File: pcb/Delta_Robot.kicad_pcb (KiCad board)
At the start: 2 copper layers, 151 parts, among them J1 Conn_01x04, J2 USB_A, J3 USB_A, J4 Conn_01x02, J5 Conn_01x02, J6 MP3V5050VC6U, Q1 IRF9540STRLPBF, Q2 IRF9540STRLPBF, SW1 TL3305A, SW2 TL3305A, SW3 TL3305A, SW4 TL3305A, U1 LDL1117S33R, U2 LDL1117S33R, U3 ZLDO1117G12TA, U4 ICE40UP5K-SG48I, U5 W25Q16JVSSIQ TR, U5 W25Q64JVSSIQ, U6 STM32F412RGT6, U7 Omega2+, U8 4N25-X007T, U9 4N25-X007T, Y1 Crystal

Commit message: Organizacion basica PCB
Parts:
- removed the C16 at (174.4, 124.6)
- removed the C16 at (136.3, 168.8)
- removed the C17 at (170.0, 127.1)
- removed the C17 at (145.6, 157.0)
- removed the C18 at (165.7, 127.1)
- removed the C18 at (141.2, 159.5)
- removed the C19 at (177.0, 117.8)
- removed the C19 at (136.3, 166.3)
- removed the C20 at (178.8, 122.8)
- removed the C20 at (136.9, 162.0)
- removed the C21 at (174.4, 127.1)
- removed the C21 at (131.9, 168.8)
- removed the C22 at (177.0, 120.3)
- removed the C22 at (136.9, 159.5)
- removed the C23 at (170.1, 124.6)
- removed the C23 at (131.9, 166.3)
- removed the D3 at (157.0, 123.1)
- removed the D3 at (129.5, 152.4)
- removed the D5 at (76.1, 135.8)
- removed the D7 at (116.4, 54.8)
- removed the D7 at (164.3, 158.0)
- removed L11: 742792651, Inductor_SMD:L_0603_1608Metric_Pad1.05x0.95mm_HandSolder
- removed the R3 at (161.4, 124.6)
- removed the R4 at (157.0, 125.6)
- removed the R5 at (177.0, 115.3)
- removed the R6 at (165.7, 124.6)
- removed the R7 at (161.3, 127.1)
- removed the R7 at (145.6, 162.0)
- removed the SW1 at (91.4, 131.5)
- removed the SW2 at (129.7, 49.5)
- removed the SW2 at (156.9, 158.7)
- removed the SW3 at (119.4, 49.5)
- removed the U4 at (170.2, 118.7)
- removed the U5 at (160.2, 117.9)
- added C16: 0.1uF, Capacitor_SMD:C_0603_1608Metric, F.Cu at (87.7, 93.2)
- added C17: 1uF, Capacitor_SMD:C_0603_1608Metric, F.Cu at (102.9, 69.8)
- added C18: 1uF, Capacitor_SMD:C_0603_1608Metric, F.Cu at (106.9, 81.4)
- added C19: 1uF, Capacitor_SMD:C_0603_1608Metric, F.Cu at (100.5, 85.7)
- added C20: 1uF, Capacitor_SMD:C_0603_1608Metric, F.Cu at (87.6, 73.0)
- added C21: 0.1uF, Capacitor_SMD:C_0603_1608Metric, F.Cu at (99.9, 69.8)
- added C22: 0.1uF, Capacitor_SMD:C_0603_1608Metric, F.Cu at (106.9, 78.5)
- added C23: 10uF, Capacitor_SMD:C_0603_1608Metric, F.Cu at (106.9, 87.4)
- added C51: 100nF, Capacitor_SMD:C_0603_1608Metric, F.Cu at (53.0, 44.2)
- added C52: 100nF, Capacitor_SMD:C_0603_1608Metric, F.Cu at (48.5, 44.2)
- added C53: 1uF, Capacitor_SMD:C_0603_1608Metric, F.Cu at (57.4, 44.2)
- added D3: CDBU0520, Diode_SMD:D_0603_1608Metric, F.Cu at (103.0, 85.7)
- added D7: NUP2105L, Package_TO_SOT_SMD:SOT-23, F.Cu at (113.3, 43.2)
- added J7: RJ45, Connector_RJ:RJ45_Amphenol_RJHSE5380, F.Cu at (56.8, 30.5)
- added R32: 50, Resistor_SMD:R_0603_1608Metric, F.Cu at (54.5, 40.9)
- added R33: 50, Resistor_SMD:R_0603_1608Metric, F.Cu at (48.5, 40.9)
- added R34: 50, Resistor_SMD:R_0603_1608Metric, F.Cu at (51.6, 40.9)
- added R35: 50, Resistor_SMD:R_0603_1608Metric, F.Cu at (57.4, 40.9)
- added R7: 100, Resistor_SMD:R_0603_1608Metric, F.Cu at (106.9, 84.3)
- added SW2: TL3305A, Button_Switch_SMD:SW_SPST_TL3305A, F.Cu at (120.9, 65.4)
- C1, C2, C24, C25, C26, C27, C28, C29, C30, C31, C34, C35, C38, C39, C40, C42, C43, C44, C45, C46, C47, C48, C49, C50, C7, C8: footprint Capacitor_SMD:C_0603_1608Metric_Pad1.05x0.95mm_HandSolder -> Capacitor_SMD:C_0603_1608Metric
- C10, C11: value 220u -> 220uF; footprint Capacitor_SMD:C_0603_1608Metric_Pad1.05x0.95mm_HandSolder -> Capacitor_SMD:C_0603_1608Metric
- C12, C13, C33, C36, C37, C4, C5, C6: value 0.1u -> 0.1uF; footprint Capacitor_SMD:C_0603_1608Metric_Pad1.05x0.95mm_HandSolder -> Capacitor_SMD:C_0603_1608Metric
- C14, C15: value 1n -> 1nF; footprint Capacitor_SMD:C_0603_1608Metric_Pad1.05x0.95mm_HandSolder -> Capacitor_SMD:C_0603_1608Metric
- C3, C9: value 33u -> 33uF; footprint Capacitor_SMD:C_0603_1608Metric_Pad1.05x0.95mm_HandSolder -> Capacitor_SMD:C_0603_1608Metric
- C32: value 22u -> 22uF; footprint Capacitor_SMD:C_0603_1608Metric_Pad1.05x0.95mm_HandSolder -> Capacitor_SMD:C_0603_1608Metric
- C41: value 0.01uF -> 10nF; footprint Capacitor_SMD:C_0603_1608Metric_Pad1.05x0.95mm_HandSolder -> Capacitor_SMD:C_0603_1608Metric
- D1, D10, D2, D8: footprint LED_SMD:LED_0603_1608Metric_Pad1.05x0.95mm_HandSolder -> LED_SMD:LED_0603_1608Metric
- D11, D9: footprint Diode_SMD:D_0603_1608Metric_Pad1.05x0.95mm_HandSolder -> Diode_SMD:D_0603_1608Metric
- L1, L10, L2, L3, L4, L5, L6: footprint Inductor_SMD:L_0603_1608Metric_Pad1.05x0.95mm_HandSolder -> Inductor_SMD:L_0603_1608Metric
- R1, R10, R11, R12, R13, R14, R15, R16, R17, R18, R19, R2, R20, R21, R22, R23, R24, R25, R26, R27, R29, R30, R31, R8, R9: footprint Resistor_SMD:R_0603_1608Metric_Pad1.05x0.95mm_HandSolder -> Resistor_SMD:R_0603_1608Metric
- U7: footprint Module:Onion_Omega2+ -> TH:ONION_OMEGA2
- moved H2 211.6 mm to (17.8, 25.4), turned to 180 degrees
- moved H4 202.7 mm to (17.4, 92.8)
- moved R25 201.1 mm to (25.4, 81.7)
- moved L10 196.8 mm to (18.0, 84.8), turned to 180 degrees
- moved R22 195.3 mm to (37.0, 81.7)
- moved R21 195.2 mm to (35.4, 62.6)
- moved R24 194.7 mm to (35.4, 59.6), turned to 180 degrees
- moved R23 194.6 mm to (35.5, 53.2)
- moved J4 184.4 mm to (38.6, 90.3)
- moved J5 183.7 mm to (27.1, 90.3)
- moved R20 181.2 mm to (48.9, 53.2)
- moved U9 180.2 mm to (28.4, 57.9), turned to 180 degrees
- moved U8 176.1 mm to (42.4, 57.9), turned to 180 degrees
- moved C13 169.1 mm to (59.1, 82.2), turned to 90 degrees
- moved D12 168.5 mm to (28.6, 42.7), turned to 270 degrees
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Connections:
- C11 pad 1: +24V -> GNDPWR
- C11 pad 2: GNDPWR -> +24V
- C13 pad 1: +24V -> GNDPWR
- C13 pad 2: GNDPWR -> +24V
- C15 pad 1: +24V -> GNDPWR
- C15 pad 2: GNDPWR -> +24V
- D2 pad 1: GND -> GNDPWR
- D5 pad 2: Net-(D5-Pad2) -> /FPGA/FPGA_CDONE
- J1 pad 1: GNDPWR -> +24V
- J1 pad 2: +24V -> GNDPWR
- J2 pad 5: Net-(J2-Pad5) -> GND_CASE
- J4 pad 1: Net-(D9-Pad1) -> GNDPWR
- J4 pad 2: GNDPWR -> Net-(D9-Pad1)
- J6 pad 1: Net-(J6-Pad1) -> (no net)
- J6 pad 5: Net-(J6-Pad5) -> (no net)
- J6 pad 6: Net-(J6-Pad6) -> (no net)
- J6 pad 7: Net-(J6-Pad7) -> (no net)
- J6 pad 8: Net-(J6-Pad8) -> (no net)
- L5 pad 1: +5V_USB_STM32 -> (no net)
- L8 pad 1: +5V_USB_OMEGA2+ -> (no net)
- R11 pad 2: /Onion Omega 2/OMEGA2_SPI_MISO -> (no net)
- R12 pad 2: /Onion Omega 2/OMEGA2_SPI_MOSI -> (no net)
- R13 pad 2: /Onion Omega 2/OMEGA2_SPI_CLK -> (no net)
- R14 pad 2: /Onion Omega 2/OMEGA2_SPI_CS -> (no net)
- R15 pad 2: /Onion Omega 2/OMEGA2_SPI_RST -> (no net)
- R28 pad 1: Net-(D5-Pad2) -> /FPGA/FPGA_CDONE
- R28 pad 2: /FPGA/FPGA_CDONE -> +3V3_FPGA
- U4 pad 10: /FPGA/FPGA_CTRL_NWAIT -> (no net)
- U4 pad 11: /FPGA/FPGA_CTRL_NE -> (no net)
- U4 pad 12: /FPGA/FPGA_CTRL_NAVD -> (no net)
- U4 pad 13: Net-(U4-Pad13) -> (no net)
- U4 pad 16: /FPGA/FPGA_SPI_SS -> (no net)
- U4 pad 18: Net-(U4-Pad18) -> (no net)
- U4 pad 19: Net-(U4-Pad19) -> (no net)
- U4 pad 2: Net-(U4-Pad2) -> (no net)
- U4 pad 20: /FPGA/FPGA_CTRL_FMC_CLK -> (no net)
- U4 pad 21: Net-(U4-Pad21) -> (no net)
- U4 pad 23: /FPGA/FPGA_SOLENOID1 -> (no net)
- U4 pad 25: /FPGA/FPGA_SOLENOID2 -> (no net)
- U4 pad 26: Net-(U4-Pad26) -> (no net)
- U4 pad 27: Net-(U4-Pad27) -> (no net)
- U4 pad 28: Net-(U4-Pad28) -> (no net)
- U4 pad 3: Net-(U4-Pad3) -> (no net)
- U4 pad 31: Net-(U4-Pad31) -> (no net)
- U4 pad 32: Net-(U4-Pad32) -> (no net)
- U4 pad 34: Net-(U4-Pad34) -> (no net)
- U4 pad 35: Net-(U4-Pad35) -> (no net)
- U4 pad 36: Net-(U4-Pad36) -> (no net)
- U4 pad 37: Net-(U4-Pad37) -> (no net)
- U4 pad 38: Net-(U4-Pad38) -> (no net)
- U4 pad 39: Net-(U4-Pad39) -> (no net)
- U4 pad 4: Net-(U4-Pad4) -> (no net)
- U4 pad 40: Net-(U4-Pad40) -> (no net)
- U4 pad 41: Net-(U4-Pad41) -> (no net)
- U4 pad 42: Net-(U4-Pad42) -> (no net)
- U4 pad 43: Net-(U4-Pad43) -> (no net)
- U4 pad 44: Net-(U4-Pad44) -> (no net)
- U4 pad 45: Net-(U4-Pad45) -> (no net)
- U4 pad 46: Net-(U4-Pad46) -> (no net)
- U4 pad 47: Net-(U4-Pad47) -> /FPGA/FPGA_SOLENOID1
- U4 pad 48: Net-(U4-Pad48) -> /FPGA/FPGA_SOLENOID2
- U4 pad 6: /FPGA/FPGA_CTRL_NOE -> (no net)
- U4 pad 9: /FPGA/FPGA_CTRL_NWE -> (no net)
- U6 pad 1: Net-(U6-Pad1) -> (no net)
- U6 pad 10: /STM32/STM32_CTRL_NWE -> (no net)
- U6 pad 11: /STM32/STM32_CTRL_NWAIT -> (no net)
- U6 pad 13: Net-(U6-Pad13) -> (no net)
- U6 pad 14: /STM32/PRESSURE_AIN -> (no net)
- U6 pad 15: Net-(U6-Pad15) -> (no net)
- U6 pad 16: Net-(U6-Pad16) -> (no net)
- U6 pad 17: Net-(U6-Pad17) -> /STM32/PRESSURE_AIN
- U6 pad 2: Net-(U6-Pad2) -> (no net)
- U6 pad 20: Net-(U6-Pad20) -> (no net)
- U6 pad 21: Net-(U6-Pad21) -> (no net)
- U6 pad 22: Net-(U6-Pad22) -> (no net)
- U6 pad 23: Net-(U6-Pad23) -> (no net)
- U6 pad 24: /STM32/STM32_CTRL_NE -> (no net)
- U6 pad 25: Net-(U6-Pad25) -> (no net)
- U6 pad 26: Net-(U6-Pad26) -> (no net)
- U6 pad 27: Net-(U6-Pad27) -> (no net)
- U6 pad 28: Net-(U6-Pad28) -> (no net)
- U6 pad 29: Net-(U6-Pad29) -> (no net)
- U6 pad 3: Net-(U6-Pad3) -> (no net)
- U6 pad 33: Net-(U6-Pad33) -> (no net)
- U6 pad 34: Net-(U6-Pad34) -> (no net)
- U6 pad 35: Net-(U6-Pad35) -> (no net)
- U6 pad 36: Net-(U6-Pad36) -> (no net)
- U6 pad 37: Net-(U6-Pad37) -> (no net)
- U6 pad 38: Net-(U6-Pad38) -> (no net)
- U6 pad 39: Net-(U6-Pad39) -> (no net)
- U6 pad 4: Net-(U6-Pad4) -> (no net)
- U6 pad 40: Net-(U6-Pad40) -> (no net)
- U6 pad 41: Net-(U6-Pad41) -> (no net)
- U6 pad 46: /STM32/STM32_JTAG_TMS -> (no net)
- U6 pad 49: /STM32/STM32_JTAG_TCK -> (no net)
- U6 pad 50: /STM32/STM32_JTAG_TDI -> (no net)
- U6 pad 51: Net-(U6-Pad51) -> (no net)
- U6 pad 52: Net-(U6-Pad52) -> (no net)
- U6 pad 53: Net-(U6-Pad53) -> (no net)
- U6 pad 54: Net-(U6-Pad54) -> (no net)
- U6 pad 55: /STM32/STM32_JTAG_TDO -> (no net)
- U6 pad 56: /STM32/STM32_JTAG_TRST -> (no net)
- U6 pad 57: Net-(U6-Pad57) -> (no net)
- U6 pad 58: /STM32/STM32_I2C_SCL -> (no net)
- U6 pad 59: /STM32/STM32_I2C_SDA -> (no net)
- U6 pad 60: Net-(U6-Pad60) -> (no net)
- U6 pad 61: Net-(U6-Pad61) -> (no net)
- U6 pad 62: Net-(U6-Pad62) -> (no net)
- U6 pad 8: /STM32/STM32_CTRL_NAVD -> (no net)
- U6 pad 9: /STM32/STM32_CTRL_NOE -> (no net)
- U7 pad 15: Net-(U7-Pad15) -> (no net)
- U7 pad 17: /Onion Omega 2/OMEGA2_I2C_SCA -> (no net)
- U7 pad 18: /Onion Omega 2/OMEGA2_I2C_SCL -> (no net)
- U7 pad 19: /Onion Omega 2/OMEGA2_JTAG_TRST -> (no net)
- U7 pad 2: /Onion Omega 2/OMEGA2_JTAG_TMS -> (no net)
- U7 pad 20: /Onion Omega 2/OMEGA2_JTAG_NRST -> (no net)
- U7 pad 21: Net-(U7-Pad21) -> /Onion Omega 2/OMEGA2_ETH_RX+
- U7 pad 22: Net-(U7-Pad22) -> /Onion Omega 2/OMEGA2_ETH_RX-
- U7 pad 23: Net-(U7-Pad23) -> /Onion Omega 2/OMEGA2_ETH_TX+
- U7 pad 24: Net-(U7-Pad24) -> /Onion Omega 2/OMEGA2_ETH_TX-
- U7 pad 25: Net-(U7-Pad25) -> /Onion Omega 2/ETH_PWR
- U7 pad 27: Net-(U7-Pad27) -> (no net)
- U7 pad 28: Net-(U7-Pad28) -> (no net)
- U7 pad 3: Net-(U7-Pad3) -> (no net)
- U7 pad 4: Net-(U7-Pad4) -> (no net)
- U7 pad 5: /Onion Omega 2/OMEGA2_JTAG_TCK -> (no net)
- U7 pad 6: /Onion Omega 2/OMEGA2_JTAG_TDI -> (no net)
- U7 pad 7: /Onion Omega 2/OMEGA2_JTAG_TDO -> (no net)
- U8 pad 3: Net-(U8-Pad3) -> (no net)
- U8 pad 6: Net-(U8-Pad6) -> (no net)
- U9 pad 3: Net-(U9-Pad3) -> (no net)
- U9 pad 6: Net-(U9-Pad6) -> (no net)
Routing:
- net /Onion Omega 2/OMEGA2_ETH_TX-: track 0.00 -> 74.8 mm, vias 0 -> 2
- net /FPGA/FPGA_SOLENOID2: track 0.00 -> 70.9 mm
- net /FPGA/FPGA_SOLENOID1: track 0.00 -> 58.1 mm
- net /Onion Omega 2/OMEGA2_ETH_TX+: track 0.00 -> 53.9 mm
- net /Onion Omega 2/OMEGA2_USB_D+: track 0.00 -> 49.4 mm
- net /Onion Omega 2/OMEGA2_USB_D-: track 0.00 -> 42.3 mm
- net /Onion Omega 2/ETH_PWR: track 0.00 -> 33.3 mm, vias 0 -> 1
- net /Onion Omega 2/ONION_SER1_TX: track 0.00 -> 32.1 mm
- net /Onion Omega 2/ONION_SER1_RX: track 0.00 -> 30.5 mm
- net /STM32/PRESSURE_AIN: track 0.00 -> 27.9 mm
- net /Onion Omega 2/OMEGA2_FW_RST: track 0.00 -> 27.7 mm, vias 0 -> 1
- net /Onion Omega 2/OMEGA2_ETH_RX-: track 0.00 -> 27.2 mm, vias 0 -> 2
- net Net-(D11-Pad1): track 0.00 -> 27.1 mm
- net Net-(D9-Pad1): track 0.00 -> 26.4 mm
- net /Onion Omega 2/OMEGA2_ETH_RX+: track 0.00 -> 24.9 mm
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
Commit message: Modificacion general PCB
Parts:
- removed C1: 1uF, Capacitor_SMD:C_0603_1608Metric
- removed C33, C4: 0.1uF, Capacitor_SMD:C_0603_1608Metric
- removed C7: 4.7uF, Capacitor_SMD:C_0603_1608Metric
- removed D7: NUP2105L, Package_TO_SOT_SMD:SOT-23
- removed L1: BLM18SG121TN1D, Inductor_SMD:L_0603_1608Metric
- removed L4, L6: SRF2012-900YA, Inductor_SMD:L_0603_1608Metric
- removed L5: 742792651, Inductor_SMD:L_0603_1608Metric
- removed SW1, SW2: TL3305A, Button_Switch_SMD:SW_SPST_TL3305A
- removed U1: LDL1117S33R, Package_TO_SOT_SMD:SOT-223-3_TabPin2
- added C54: 2pF, Capacitor_SMD:C_0603_1608Metric, B.Cu at (108.1, 90.6)
- added C55: 0.1uF, Capacitor_SMD:C_0603_1608Metric, B.Cu at (114.3, 75.1)
- added CR1: ESDA6V1BC6, SMD:ESDA6V1BC6, F.Cu at (104.4, 80.8)
- added IC1: STMPS2151STR, SMD:SOT95P280X145-5N, F.Cu at (109.5, 70.4)
- added J8: 47590-0001, SMD:MOLEX_47590-0001, F.Cu at (109.5, 62.0)
- added J9: Conn_01x02, TerminalBlock_TE-Connectivity:TerminalBlock_TE_282834-2_1x02_P2.54mm_Horizontal, F.Cu at (146.7, 119.0)
- added L11: SRF2012-900YA, Inductor_SMD:L_0603_1608Metric, B.Cu at (98.5, 88.1)
- added Y2: 32.768KHZ, Crystal:Crystal_SMD_3215-2Pin_3.2x1.5mm, B.Cu at (108.6, 88.6)
- C10, C11, C12, C13, C14, C15, C16, C17, C18, C19, C2, C20, C21, C22, C23, C27, C28, C29, C3, C30, C31, C36, C37, C43, C44, C45, C46, C47, C48, C49, C5, C50, C51, C52, C53, C6, C8, C9, D3, L2, L3, R11, R12, R13, R14, R21, R24, R26, R27, R29, R3, R30, R31, R32, R33, R34, R35, R4, R5, R6, R7, U2, U3, U4, U5, U6, U8, U9: moved to B.Cu
- C24, C25: value 0.1uF -> 4.3pF; moved to B.Cu
- C26: value 0.1uF -> 4.7uF; footprint Capacitor_SMD:C_0603_1608Metric -> Capacitor_SMD:CP_Elec_4x3
- C32: footprint Capacitor_SMD:C_0603_1608Metric -> Capacitor_SMD:CP_Elec_4x3
- C34: value 22u -> 2pF; moved to B.Cu
- D4: value 1N4733AW -> LED; footprint Diode_SMD:D_SOD-123 -> LED_SMD:LED_0603_1608Metric
- D5: footprint LED_SMD:LED_0603_1608Metric_Pad1.05x0.95mm_HandSolder -> LED_SMD:LED_0603_1608Metric; moved to B.Cu
- H1, H2, H3, H4: footprint MountingHole:MountingHole_3.2mm_M3_Pad -> MountingHole:MountingHole_3.2mm_M3_Pad_Via
- J1: footprint TerminalBlock_Phoenix:TerminalBlock_Phoenix_MKDS-3-4-5.08_1x04_P5.08mm_Horizontal -> TerminalBlock_TE-Connectivity:TerminalBlock_TE_282834-4_1x04_P2.54mm_Horizontal
- J2: value USB_A -> Conn_01x03; footprint Connector_USB:USB_A_Wuerth_61400826021_Horizontal_Stacked -> TerminalBlock_TE-Connectivity:TerminalBlock_TE_282834-3_1x03_P2.54mm_Horizontal
- J3: footprint Connector_USB:USB_A_Wuerth_61400826021_Horizontal_Stacked -> Connector_USB:USB_A_Stewart_SS-52100-001_Horizontal
- J4, J5: footprint TerminalBlock_Phoenix:TerminalBlock_Phoenix_MKDS-3-2-5.08_1x02_P5.08mm_Horizontal -> TerminalBlock_TE-Connectivity:TerminalBlock_TE_282834-2_1x02_P2.54mm_Horizontal
- L7, L8, L9: footprint Inductor_SMD:L_0603_1608Metric_Pad1.05x0.95mm_HandSolder -> Inductor_SMD:L_0603_1608Metric
- R10: value 0K -> 620
- R20, R23: value 100 -> 330; moved to B.Cu
- R28: footprint Resistor_SMD:R_0603_1608Metric_Pad1.05x0.95mm_HandSolder -> Resistor_SMD:R_0603_1608Metric; moved to B.Cu
- R9: value 0K -> 10k
- Y1: value Crystal -> 8MHz; footprint Crystal:Crystal_C38-LF_D3.0mm_L8.0mm_Vertical -> Crystal:Crystal_SMD_HC49-SD; moved to B.Cu
- moved J5 153.8 mm to (180.2, 104.4), turned to 90 degrees
- moved R25 151.4 mm to (174.2, 109.7), turned to 90 degrees
- moved D10 146.6 mm to (174.2, 105.6), turned to 270 degrees
- moved U9 145.8 mm to (166.5, 104.9), turned to 90 degrees
- moved R21 144.4 mm to (171.2, 111.9), turned to 270 degrees
- moved J4 143.5 mm to (180.2, 113.7), turned to 90 degrees
- moved R22 142.9 mm to (174.2, 121.3), turned to 90 degrees
- moved R24 142.7 mm to (168.1, 111.9), turned to 90 degrees
- moved D11 141.9 mm to (174.2, 101.4), turned to 270 degrees
- moved C35 141.7 mm to (173.6, 78.1), turned to 180 degrees
- moved L8 141.1 mm to (177.8, 78.1)
- moved J3 140.7 mm to (172.5, 73.0)
- moved D6 139.6 mm to (172.7, 75.9)
- moved Q2 139.3 mm to (164.8, 105.5), turned to 0 degrees
- moved L7 139.0 mm to (166.8, 77.3)
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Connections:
- C16 pad 1: +3V3_FPGA -> +3V3
- C26 pad 1: Net-(C26-Pad1) -> /STM32/STM32_USB_VBUS
- C27 pad 1: +3.3V_ESP32 -> +3V3
- C29 pad 1: +3.3V_ESP32 -> +3V3
- C30 pad 1: +3.3V_ESP32 -> +3V3
- C31 pad 1: +3.3V_ESP32 -> +3V3
- C35 pad 1: Net-(C34-Pad1) -> Net-(C32-Pad1)
- C36 pad 1: +3V3_OMEGA2+ -> +3V3
- C37 pad 1: +3V3_OMEGA2+ -> +3V3
- C40 pad 1: +3.3V_ESP32 -> +3V3
- C41 pad 1: +3.3V_ESP32 -> +3V3
- C5 pad 1: +3V3_FPGA -> +3V3
- C50 pad 1: +3V3_FPGA -> +3V3
- C8 pad 1: +3V3_FPGA -> +3V3
- D3 pad 2: +3V3_FPGA -> +3V3
- D4 pad 1: Net-(C32-Pad1) -> /STM32/STM32_USB_OverCurrent
- D4 pad 2: GND -> Net-(D4-Pad2)
- D6 pad 1: Net-(C34-Pad1) -> Net-(C32-Pad1)
- J1 pad 1: +24V -> +5V
- J1 pad 2: GNDPWR -> GND
- J1 pad 3: GND -> GNDPWR
- J1 pad 4: +5V -> +24V
- J2 pad 1: GND -> /External Communications/EXT_RS232_TX
- J2 pad 2: Net-(D7-Pad1) -> /External Communications/EXT_RS232_RX
- J2 pad 3: Net-(D7-Pad2) -> GND
- J6 pad 2: +3.3V_ESP32 -> +3V3
- L8 pad 1: (no net) -> +5V
- L8 pad 2: Net-(C34-Pad1) -> Net-(C32-Pad1)
- R10 pad 1: Net-(L4-Pad1) -> Net-(D4-Pad2)
- R10 pad 2: /STM32/STM32_USB_D- -> +3V3
- R18 pad 1: +3V3_OMEGA2+ -> +3V3
- R19 pad 1: +3V3_OMEGA2+ -> +3V3
- R27 pad 2: +3V3_FPGA -> +3V3
- R28 pad 2: +3V3_FPGA -> +3V3
- R3 pad 1: +3V3_FPGA -> +3V3
- R30 pad 2: +3V3_FPGA -> +3V3
- R31 pad 2: +3V3_FPGA -> +3V3
- R5 pad 1: +3V3_FPGA -> +3V3
- R6 pad 1: +3V3_FPGA -> +3V3
- R8 pad 1: Net-(C26-Pad1) -> GND
- R8 pad 2: +3.3V_ESP32 -> /STM32/STM32_USB_PowerSwitchOn
- R9 pad 1: /STM32/STM32_USB_D+ -> /STM32/STM32_USB_OverCurrent
- R9 pad 2: Net-(L6-Pad1) -> +3V3
- U2 pad 2: +3V3_FPGA -> +3V3
- U4 pad 25: (no net) -> /FPGA/FPGA_SOLENOID1
- U4 pad 26: (no net) -> /FPGA/FPGA_SOLENOID2
- U4 pad 47: /FPGA/FPGA_SOLENOID1 -> (no net)
- U4 pad 48: /FPGA/FPGA_SOLENOID2 -> (no net)
- U4 pad 8: /FPGA/FPGA_CRESET_B -> /FPGA/~FPGA_CRESET_B
- U5 pad 8: +3V3_FPGA -> +3V3
- U6 pad 13: (no net) -> Net-(L11-Pad2)
- U6 pad 19: +3.3V_ESP32 -> +3V3
- U6 pad 3: (no net) -> Net-(C34-Pad1)
- U6 pad 32: +3.3V_ESP32 -> +3V3
- U6 pad 4: (no net) -> Net-(C54-Pad1)
- U6 pad 40: (no net) -> /STM32/STM32_USB_OverCurrent
- U6 pad 42: /Onion Omega 2/ONION_SER1_RX -> /STM32/STM32_USB_VBUS
- U6 pad 43: /Onion Omega 2/ONION_SER1_TX -> /STM32/STM32_USB_ID
- U6 pad 44: /STM32/STM32_USB_D+ -> /STM32/STM32_USB_DM
- U6 pad 45: /STM32/STM32_USB_D- -> /STM32/STM32_USB_DP
- U6 pad 46: (no net) -> /STM32/STM32_USB_PowerSwitchOn
- U6 pad 48: +3.3V_ESP32 -> +3V3
- U6 pad 51: (no net) -> /Onion Omega 2/ONION_SER1_RX
- U6 pad 52: (no net) -> /Onion Omega 2/ONION_SER1_TX
- U6 pad 64: +3.3V_ESP32 -> +3V3
- U6 pad 7: Net-(C26-Pad1) -> /Onion Omega 2/STM32_NRST
- U7 pad 20: (no net) -> /FPGA/~FPGA_CRESET_B
- U7 pad 27: (no net) -> /External Communications/EXT_RS232_RX
- U7 pad 28: (no net) -> /External Communications/EXT_RS232_TX
- U7 pad 31: +3V3_OMEGA2+ -> +3V3
- U7 pad 4: (no net) -> /Onion Omega 2/STM32_NRST
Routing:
- net /FPGA/FPGA_SOLENOID2: track 70.9 -> 0.00 mm
- net /FPGA/FPGA_SOLENOID1: track 58.1 -> 0.00 mm
- net /External Communications/EXT_RS232_TX: track 0.00 -> 57.5 mm
- net +24V: track 0.00 -> 54.7 mm
- net /External Communications/EXT_RS232_RX: track 0.00 -> 54.5 mm
- net /Onion Omega 2/OMEGA2_ETH_TX-: track 74.8 -> 35.2 mm, vias 2 -> 1
- net /Onion Omega 2/OMEGA2_USB_D+: track 49.4 -> 14.3 mm, vias 0 -> 1
- net /Onion Omega 2/OMEGA2_USB_D-: track 42.3 -> 10.4 mm, vias 0 -> 1
- net /Onion Omega 2/STM32_NRST: track 0.00 -> 31.6 mm, vias 0 -> 1
- net /FPGA/~FPGA_CRESET_B: track 0.00 -> 29.1 mm, vias 0 -> 1
- net /STM32/STM32_USB_VBUS: track 0.00 -> 28.2 mm, vias 0 -> 2
- net /STM32/STM32_USB_ID: track 0.00 -> 27.1 mm, vias 0 -> 1
- net /Onion Omega 2/OMEGA2_ETH_TX+: track 53.9 -> 28.6 mm
- net +5V: track 0.00 -> 23.9 mm, vias 0 -> 1
- net /STM32/STM32_USB_DP: track 0.00 -> 20.2 mm, vias 0 -> 2
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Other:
- board outline added: 95.2 x 68.6 mm

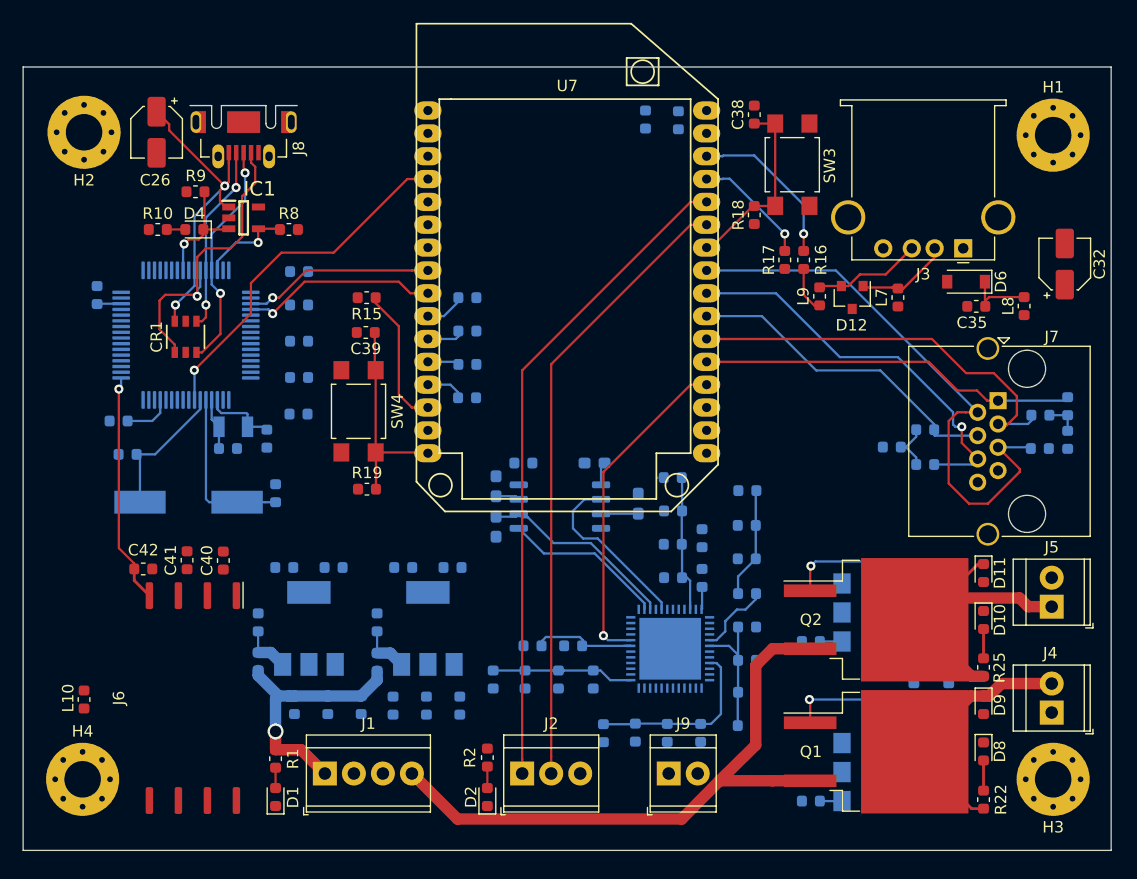
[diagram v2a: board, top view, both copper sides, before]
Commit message: Adicion zona GND
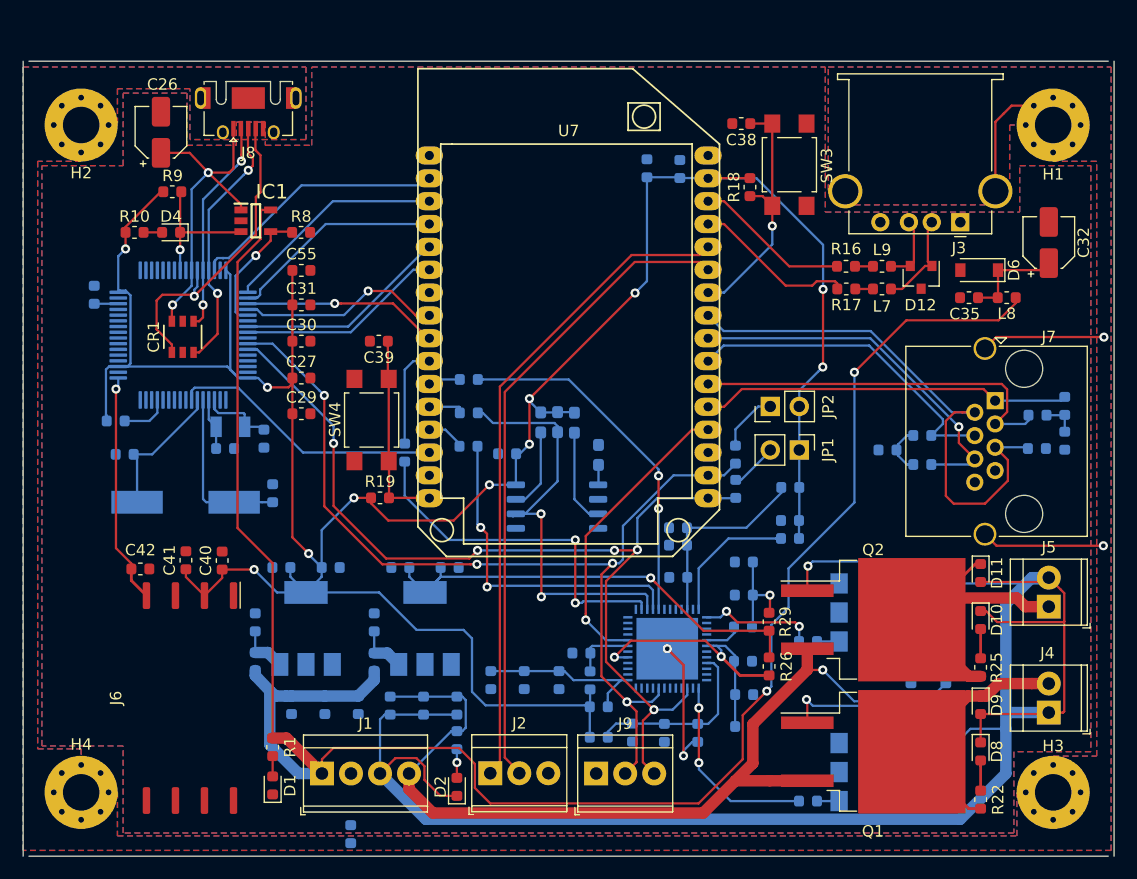
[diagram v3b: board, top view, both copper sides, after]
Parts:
- added JP1: Jumper, Connector_PinHeader_2.54mm:PinHeader_1x02_P2.54mm_Vertical, F.Cu at (158.1, 90.7)
- added JP2: Jumper, Connector_PinHeader_2.54mm:PinHeader_1x02_P2.54mm_Vertical, F.Cu at (155.6, 86.9)
- added R36: 4.7k, Resistor_SMD:R_0603_1608Metric, B.Cu at (152.5, 91.1)
- C27, C29, C30, C31, C55, R26, R29: moved to F.Cu
- J8: value 47590-0001 -> USB_OTG; footprint SMD:MOLEX_47590-0001 -> Connector_USB:USB_Micro-AB_Molex_47590-0001
- J9: value Conn_01x02 -> Conn_01x03; footprint TerminalBlock_TE-Connectivity:TerminalBlock_TE_282834-2_1x02_P2.54mm_Horizontal -> TerminalBlock_TE-Connectivity:TerminalBlock_TE_282834-3_1x03_P2.54mm_Horizontal
- L10, R2: moved to B.Cu
- R15: value 100 -> 4.7k; moved to B.Cu
- moved R15 36.4 mm to (152.6, 94.1), turned to 270 degrees
- moved L10 26.1 mm to (118.8, 124.3), turned to 90 degrees
- moved R11 14.6 mm to (123.6, 90.9), turned to 270 degrees
- moved R29 11.6 mm to (155.5, 105.7), turned to 270 degrees
- moved R3 10.6 mm to (137.0, 88.2), turned to 270 degrees
- moved R30 10.3 mm to (157.3, 94.0), turned to 0 degrees
- moved R31 9.55 mm to (140.6, 113.2), turned to 180 degrees
- moved R5 9.02 mm to (138.4, 88.3)
- moved D3 8.44 mm to (157.3, 98.4), turned to 0 degrees
- moved C50 7.85 mm to (157.3, 96.9), turned to 180 degrees
- moved R6 6.82 mm to (135.5, 88.3)
- moved J9 6.35 mm to (140.3, 119.0)
- moved D12 6.28 mm to (168.8, 75.6)
- moved L9 6.06 mm to (165.4, 74.6), turned to 0 degrees
- moved R17 5.95 mm to (162.2, 76.6), turned to 180 degrees
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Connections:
- J9 pad 1: (no net) -> GND
- J9 pad 2: (no net) -> /External Communications/EXT_I2C0
- R11 pad 2: (no net) -> /FPGA/FPGA_SPI0
- R12 pad 2: (no net) -> /FPGA/FPGA_SPI1
- R13 pad 2: (no net) -> /FPGA/FPGA_SPI2
- R14 pad 2: (no net) -> /FPGA/FPGA_SPI3
- R15 pad 1: Net-(R15-Pad1) -> Net-(JP1-Pad2)
- R15 pad 2: (no net) -> /External Communications/EXT_I2C1
- R3 pad 2: /FPGA/FPGA_SPI_SCK -> /FPGA/FPGA_SPI2
- U4 pad 14: /FPGA/FPGA_SPI_SDO -> /FPGA/FPGA_SPI0
- U4 pad 15: /FPGA/FPGA_SPI_SCK -> /FPGA/FPGA_SPI2
- U4 pad 16: (no net) -> /FPGA/FPGA_SPI3
- U4 pad 17: /FPGA/FPGA_SPI_SDI -> /FPGA/FPGA_SPI1
- U4 pad 25: /FPGA/FPGA_SOLENOID1 -> /FPGA/FPGA_SOLENOID2
- U4 pad 26: /FPGA/FPGA_SOLENOID2 -> (no net)
- U4 pad 37: (no net) -> /FPGA/FPGA_SOLENOID1
- U4 pad 39: (no net) -> /External Communications/EXT_I2C1
- U4 pad 44: (no net) -> /External Communications/EXT_I2C0
- U5 pad 2: /FPGA/FPGA_SPI_SDI -> (no net)
- U5 pad 5: /FPGA/FPGA_SPI_SDO -> (no net)
- U5 pad 6: /FPGA/FPGA_SPI_SCK -> /FPGA/FPGA_SPI2
- U6 pad 46: /STM32/STM32_USB_PowerSwitchOn -> /Onion Omega 2/OMEGA2_JTAG_TMS
- U6 pad 49: (no net) -> /Onion Omega 2/OMEGA2_JTAG_TCK
- U6 pad 50: (no net) -> /Onion Omega 2/OMEGA2_JTAG_TDI
- U6 pad 51: /Onion Omega 2/ONION_SER1_RX -> /Onion Omega 2/Omega2_SER1_TX
- U6 pad 52: /Onion Omega 2/ONION_SER1_TX -> /Onion Omega 2/Omega2_SER1_RX
- U6 pad 53: (no net) -> /STM32/STM32_USB_PowerSwitchOn
- U6 pad 55: (no net) -> /Onion Omega 2/OMEGA2_JTAG_TDO
- U6 pad 56: (no net) -> /Onion Omega 2/OMEGA2_JTAG_TRST
- U6 pad 58: (no net) -> /External Communications/EXT_I2C0
- U6 pad 59: (no net) -> /External Communications/EXT_I2C1
- U7 pad 14: Net-(R15-Pad1) -> /Onion Omega 2/STM32_NRST
- U7 pad 17: (no net) -> /External Communications/EXT_I2C1
- U7 pad 18: (no net) -> /External Communications/EXT_I2C0
- U7 pad 2: (no net) -> /Onion Omega 2/OMEGA2_JTAG_TMS
- U7 pad 3: (no net) -> /Onion Omega 2/OMEGA2_JTAG_TCK
- U7 pad 4: /Onion Omega 2/STM32_NRST -> /Onion Omega 2/OMEGA2_JTAG_TDI
- U7 pad 5: (no net) -> /Onion Omega 2/OMEGA2_JTAG_TDO
- U7 pad 6: (no net) -> /Onion Omega 2/OMEGA2_JTAG_TRST
- U7 pad 8: /Onion Omega 2/ONION_SER1_RX -> /Onion Omega 2/Omega2_SER1_RX
- U7 pad 9: /Onion Omega 2/ONION_SER1_TX -> /Onion Omega 2/Omega2_SER1_TX
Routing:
- net +3V3: track 0.00 -> 242.2 mm, vias 0 -> 11
- net GNDPWR: track 0.00 -> 153.6 mm
- net +5V: track 23.9 -> 177.4 mm, vias 1 -> 2
- net /External Communications/EXT_I2C0: track 0.00 -> 85.9 mm, vias 0 -> 4
- net /External Communications/EXT_I2C1: track 0.00 -> 85.5 mm, vias 0 -> 5
- net +1V2_FPGA: track 0.00 -> 40.6 mm, vias 0 -> 1
- net /FPGA/FPGA_SPI2: track 0.00 -> 37.6 mm, vias 0 -> 2
- net GND_CASE: track 0.00 -> 34.0 mm, vias 0 -> 2
- net /FPGA/FPGA_SPI0: track 0.00 -> 31.6 mm, vias 0 -> 2
- net /FPGA/FPGA_SPI1: track 0.00 -> 31.3 mm, vias 0 -> 2
- net /FPGA/FPGA_SPI3: track 0.00 -> 29.1 mm, vias 0 -> 2
- net +24V: track 54.7 -> 82.1 mm, vias 0 -> 1
- net /Onion Omega 2/OMEGA2_JTAG_TMS: track 0.00 -> 22.7 mm
- net /Onion Omega 2/OMEGA2_JTAG_TCK: track 0.00 -> 19.5 mm
- net /Onion Omega 2/OMEGA2_JTAG_TDI: track 0.00 -> 18.9 mm
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- added copper zone on B.Cu, net GND
- added copper zone on F.Cu, net GND
- added copper zone on B.Cu, net GND_CASE
- added copper zone on F.Cu, net GND_CASE
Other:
- board size 95.2 x 68.6 mm -> 95.5 x 69.6 mm
- net class Default: trace_width 0.25 -> 0.2
